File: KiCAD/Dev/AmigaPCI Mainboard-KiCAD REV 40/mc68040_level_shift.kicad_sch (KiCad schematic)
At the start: 26 parts, among them U801 74LVC1G17, U802 SN74LVC16T245DLR, U803 SN74LVC16T245DLR, U804 SN74LVC16T245DLR, U805 SN74LVC16T245DLR, U806 74LVC245, U807 74LVC245, U808 74LVC245, U809 74LVC245, U810 74LVC245, U811 74LVC245

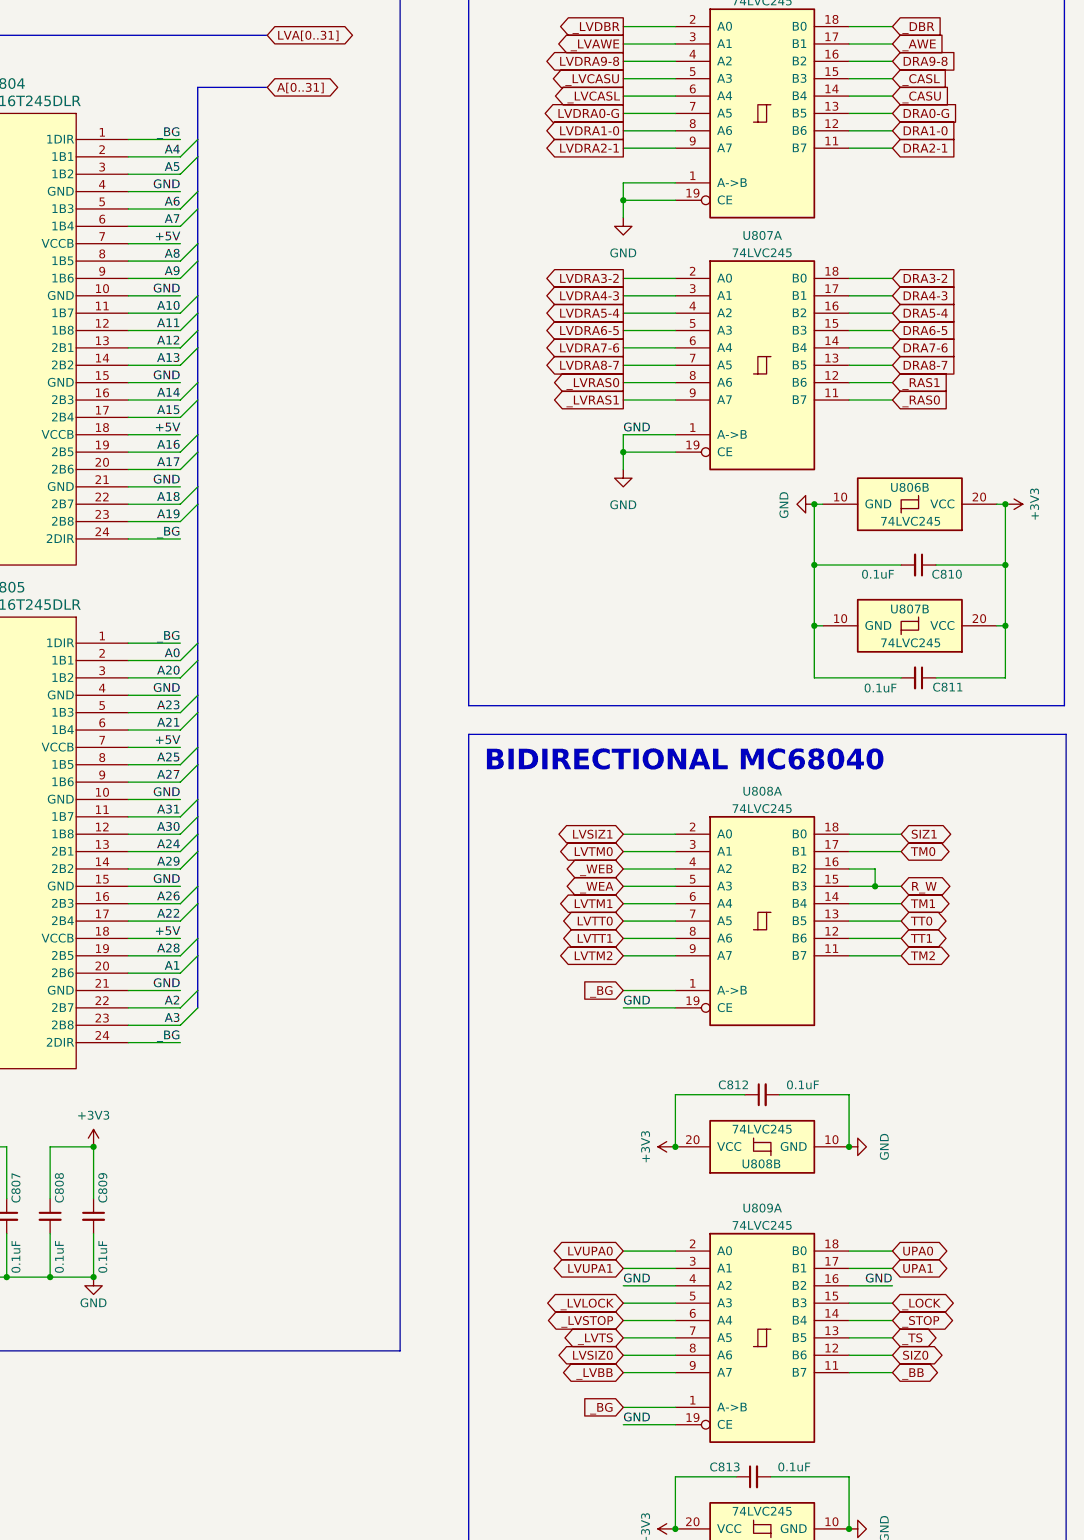
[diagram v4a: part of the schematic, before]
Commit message: AmigaPCI - Add BUSDIR signal, seperate from _BG.
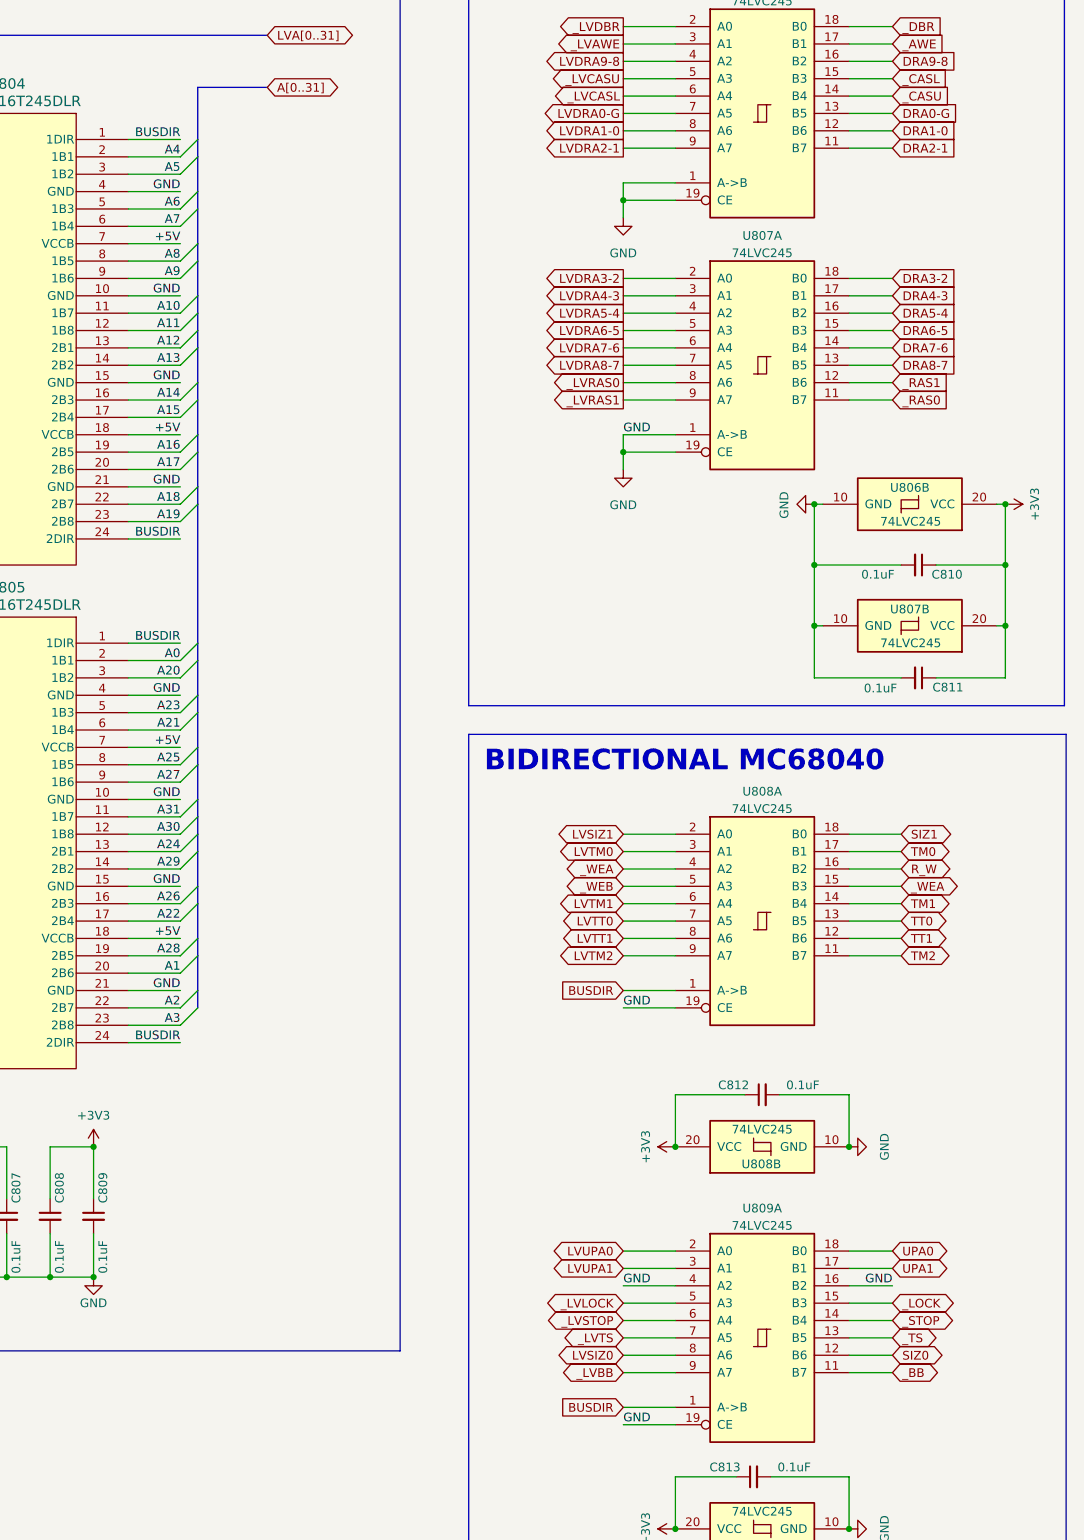
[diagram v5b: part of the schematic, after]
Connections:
- net R_W: no longer U808.15 (B3)
- net _WEA: now also U808.15 (B3), U808.4 (A2); no longer U808.5 (A3)
- net _WEB: now also U808.5 (A3); no longer U808.4 (A2)
- net _BG renamed BUSDIR
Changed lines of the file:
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@@
 		(color 0 0 0 0)
 	)
-	(junction
-		(at 271.78 160.02)
-		(diameter 0)
-		(color 0 0 0 0)
-	)
 	(bus_entry
 		(at 120.65 129.54)
@@
 		)
 	)
-	(wire
-		(pts
-			(xy 267.97 157.48) (xy 271.78 157.48)
-		)
-		(stroke
-			(width 0)
-			(type default)
-		)
-	)
 	(bus
 		(pts
@@
 		)
 	)
-	(wire
-		(pts
-			(xy 275.59 160.02) (xy 271.78 160.02)
-		)
-		(stroke
-			(width 0)
-			(type default)
-		)
-	)
 	(bus
 		(pts
@@
 	(wire
 		(pts
-			(xy 271.78 157.48) (xy 271.78 160.02)
-		)
-		(stroke
-			(width 0)
-			(type default)
-		)
-	)
-	(wire
-		(pts
 			(xy 81.28 149.86) (xy 74.93 149.86)
 		)
@@
 	(wire
 		(pts
-			(xy 271.78 160.02) (xy 267.97 160.02)
+			(xy 267.97 160.02) (xy 275.59 160.02)
 		)
 		(stroke
@@
 		)
 	)
+	(wire
+		(pts
+			(xy 275.59 157.48) (xy 267.97 157.48)
+		)
+		(stroke
+			(width 0)
+			(type default)
+		)
+	)
 	(bus
 		(pts
@@
 		)
 	)
-	(label "_BG"
+	(label "BUSDIR"
 		(at 170.18 50.8 180)
 		(fields_autoplaced yes)
@@
 		)
 	)
+	(label "GND"
+		(at 274.32 218.44 180)
+		(fields_autoplaced yes)
+		(effects
+			(font
+				(size 1.27 1.27)
+			)
+			(justify right bottom)
+		)
+	)
 	(label "A23"
 		(at 170.18 134.62 180)
@@
 		)
 	)
-	(label "_BG"
+	(label "BUSDIR"
 		(at 170.18 109.22 180)
 		(fields_autoplaced yes)
@@
 		)
 	)
+	(label "GND"
+		(at 234.95 218.44 0)
+		(fields_autoplaced yes)
+		(effects
+			(font
+				(size 1.27 1.27)
+			)
+			(justify left bottom)
+		)
+	)
 	(label "D30"
 		(at 81.28 177.8 180)
@@
 		)
 	)
-	(label "_BG"
+	(label "BUSDIR"
 		(at 170.18 124.46 180)
 		(fields_autoplaced yes)
@@
 		)
 	)
-	(label "GND"
-		(at 274.32 218.44 180)
-		(fields_autoplaced yes)
-		(effects
-			(font
-				(size 1.27 1.27)
-			)
-			(justify right bottom)
-		)
-	)
 	(label "UDB10"
 		(at 349.25 92.71 0)
@@
 		)
 	)
-	(label "_BG"
+	(label "BUSDIR"
 		(at 170.18 182.88 180)
 		(fields_autoplaced yes)
@@
 		)
 	)
-	(label "GND"
-		(at 234.95 218.44 0)
-		(fields_autoplaced yes)
-		(effects
-			(font
-				(size 1.27 1.27)
-			)
-			(justify left bottom)
-		)
-	)
 	(label "LVD5"
 		(at 31.75 71.12 0)
@@
 	(global_label "_WEB"
 		(shape bidirectional)
-		(at 234.95 157.48 180)
+		(at 234.95 160.02 180)
 		(effects
 			(font
@@
 		)
 		(property "Intersheetrefs" "${INTERSHEET_REFS}"
-			(at 226.06 157.353 0)
+			(at 226.06 159.893 0)
 			(effects
 				(font
@@
 		)
 	)
-	(global_label "_BG"
+	(global_label "BUSDIR"
 		(shape input)
 		(at 234.95 175.26 180)
@@
 		)
 		(property "Intersheetrefs" "${INTERSHEET_REFS}"
-			(at 228.4572 175.26 0)
+			(at 225.01 175.26 0)
 			(effects
 				(font
@@
 		)
 	)
+	(global_label "_WEA"
+		(shape bidirectional)
+		(at 275.59 160.02 0)
+		(effects
+			(font
+				(size 1.27 1.27)
+			)
+			(justify left)
+		)
+		(property "Intersheetrefs" "${INTERSHEET_REFS}"
+			(at 284.48 159.893 0)
+			(effects
+				(font
+					(size 1.27 1.27)
+				)
+				(justify left)
+			)
+		)
+	)
 	(global_label "_AWE"
 		(shape input)
@@
 	(global_label "R_W"
 		(shape bidirectional)
-		(at 275.59 160.02 0)
+		(at 275.59 157.48 0)
 		(effects
 			(font
@@
 		)
 		(property "Intersheetrefs" "${INTERSHEET_REFS}"
-			(at 281.813 160.02 0)
+			(at 281.813 157.48 0)
 			(effects
 				(font
@@
 		)
 	)
-	(global_label "_BG"
+	(global_label "BUSDIR"
 		(shape input)
 		(at 234.95 236.22 180)
@@
 		)
 		(property "Intersheetrefs" "${INTERSHEET_REFS}"
-			(at 228.4572 236.22 0)
+			(at 225.01 236.22 0)
 			(effects
 				(font
@@
 	(global_label "_WEA"
 		(shape bidirectional)
-		(at 234.95 160.02 180)
+		(at 234.95 157.48 180)
 		(effects
 			(font
@@
 		)
 		(property "Intersheetrefs" "${INTERSHEET_REFS}"
-			(at 226.06 159.893 0)
+			(at 226.06 157.353 0)
 			(effects
 				(font

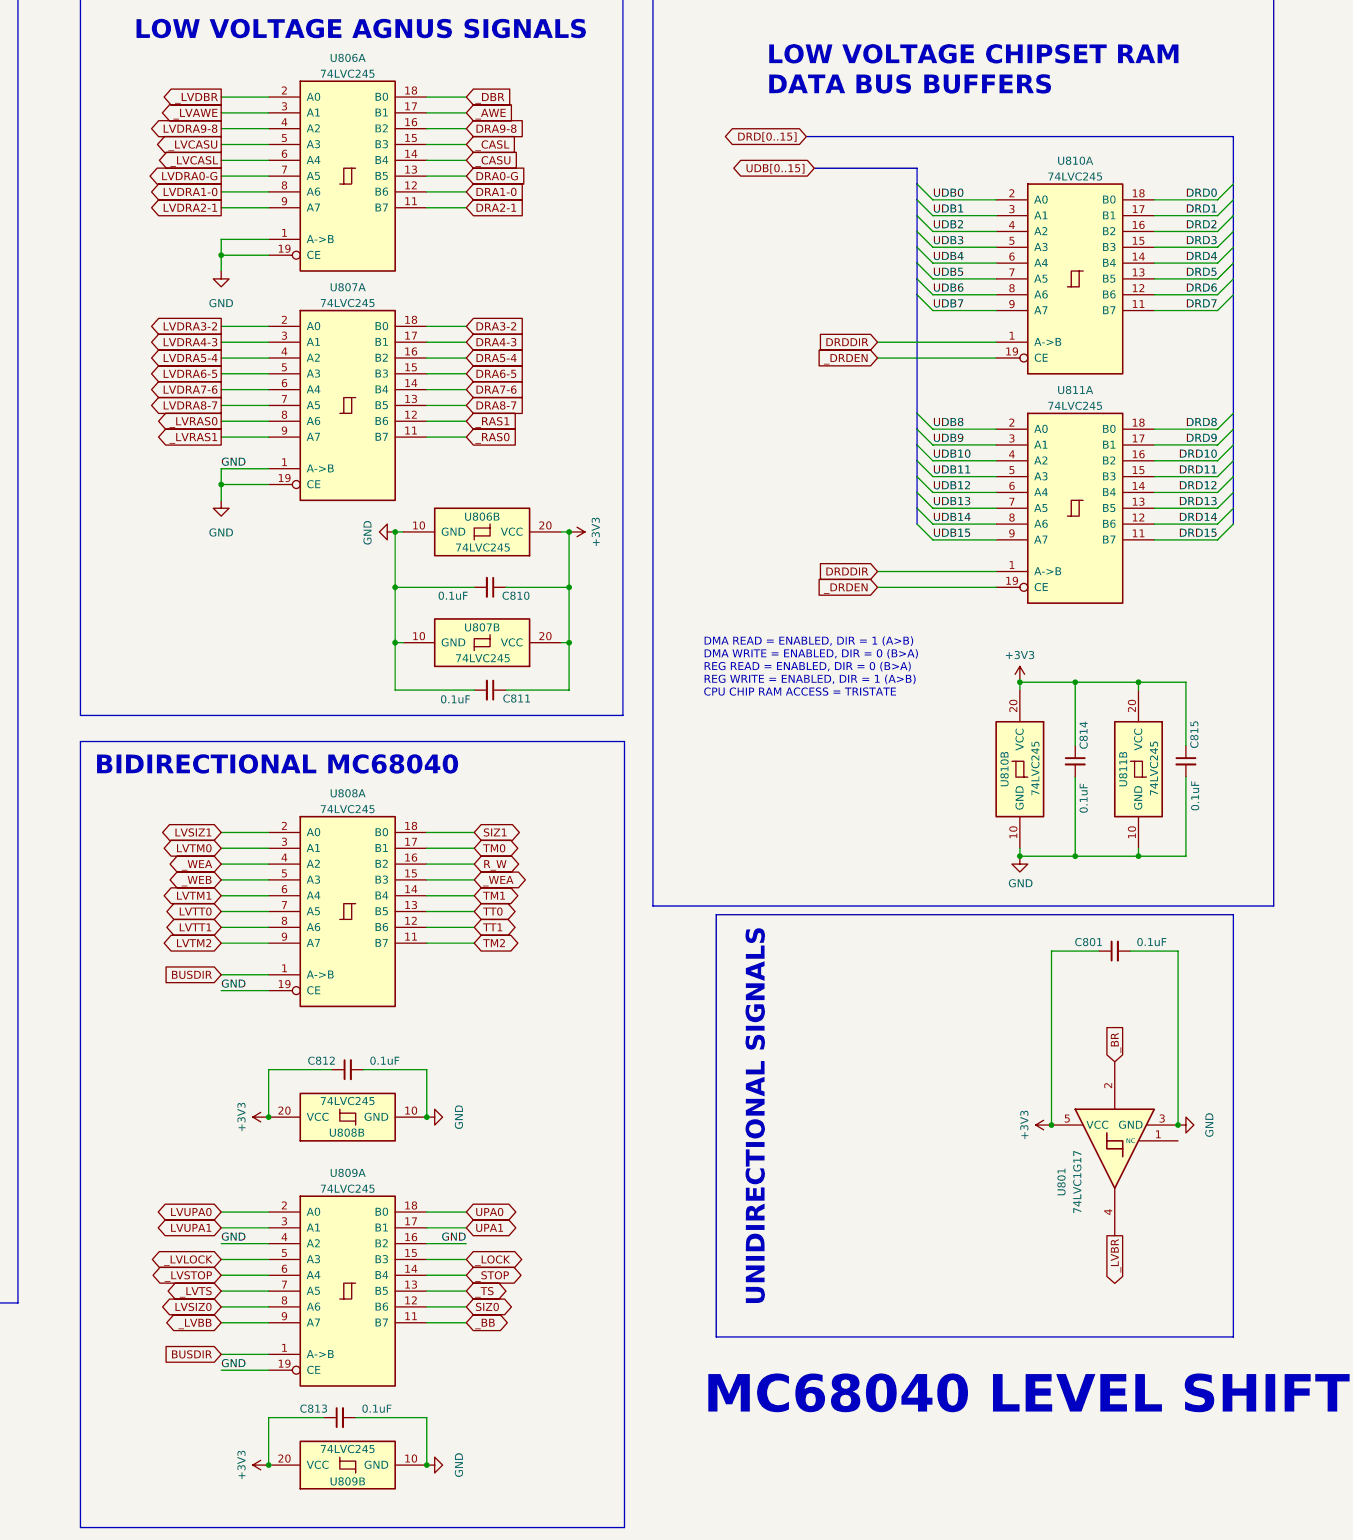
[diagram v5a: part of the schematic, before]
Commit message: AmigaPCI - swap U810 & U811 with SN74LVC16T245DLR
Drive Agnus DBR bus with TTL levels.
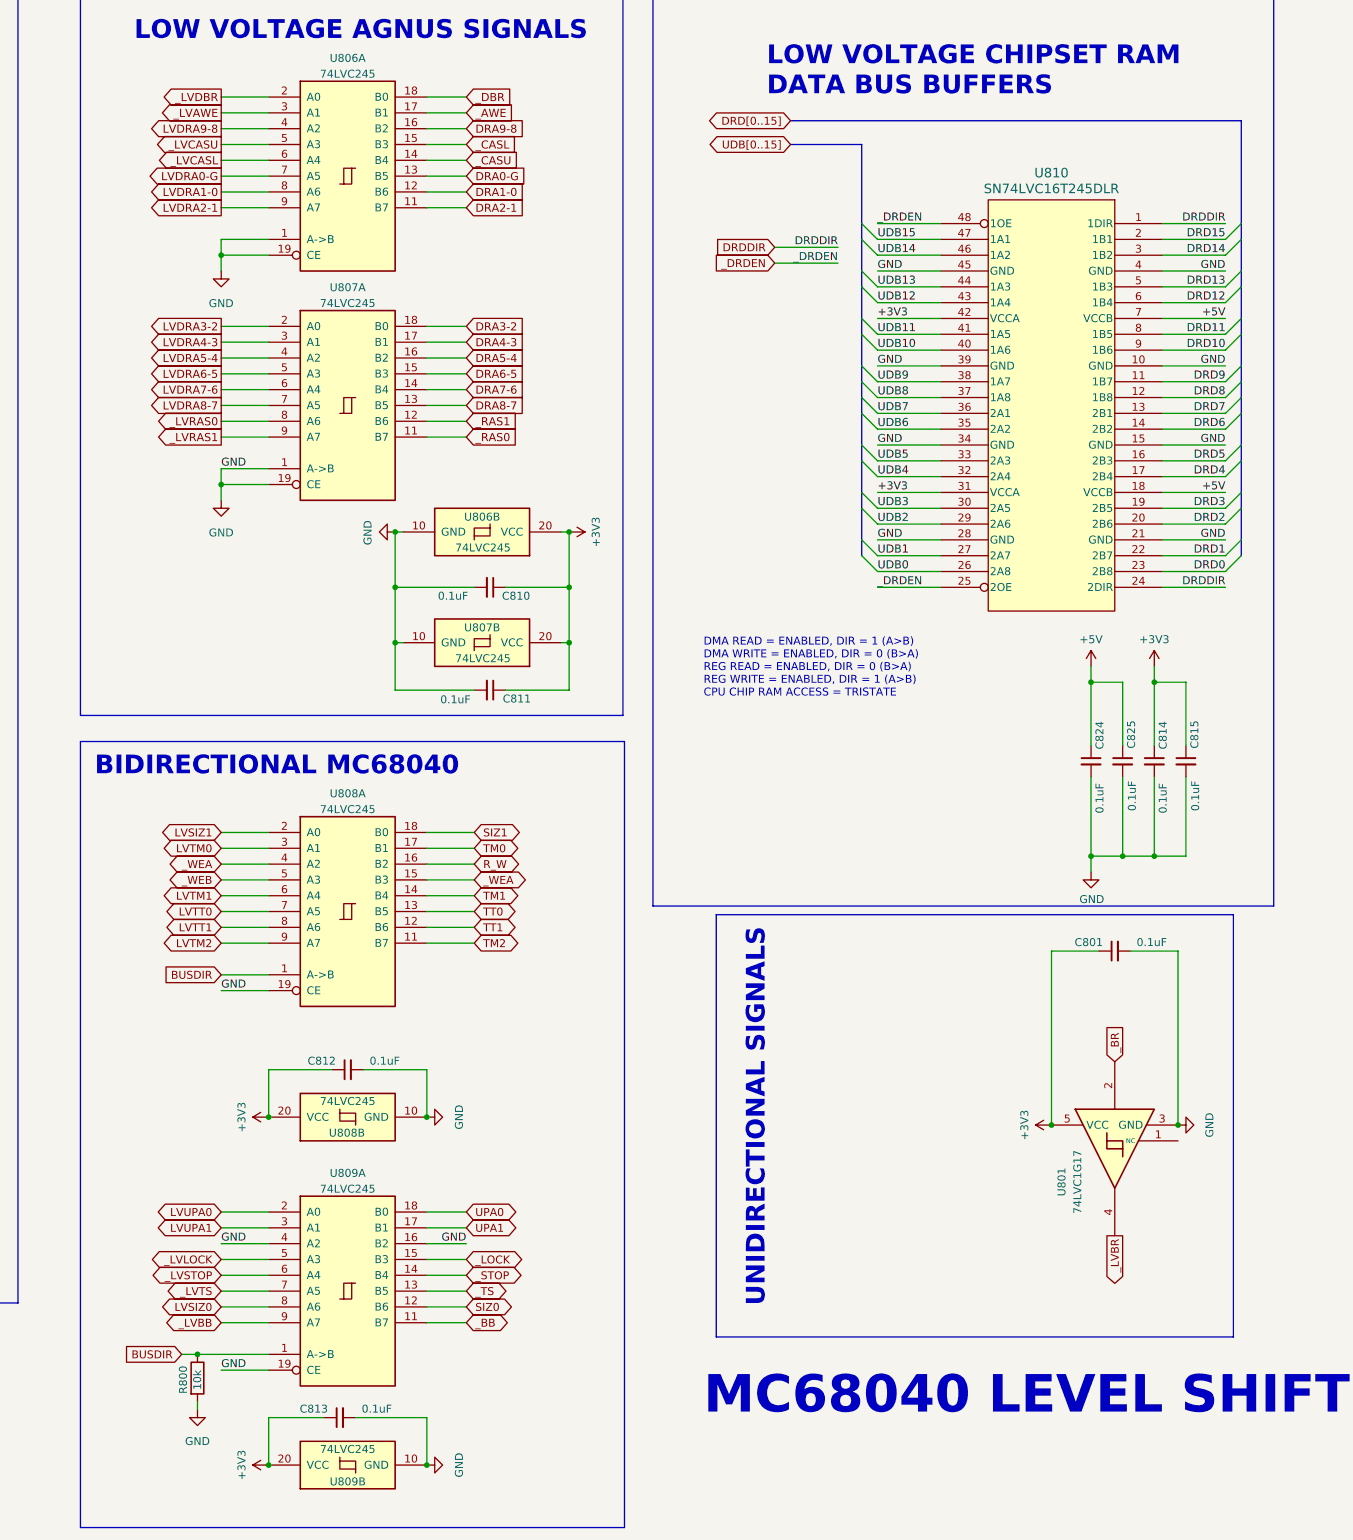
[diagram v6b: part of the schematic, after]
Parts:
- removed U810, U811: 74LVC245, Package_SO:TSSOP-20_4.4x6.5mm_P0.65mm, symbol AmigaPCI-Symbols:74LVC245
- added C824, C825: 0.1uF, Capacitor_SMD:C_0603_1608Metric, symbol Device:C_Small
- added R800: 10k, Resistor_SMD:R_0603_1608Metric, symbol Device:R
- added U810: SN74LVC16T245DLR, AmigaPCI:48-BSSOP, symbol AmigaPCI-Symbols:SN74LVC16T245DLR
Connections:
- net +3V3: now also U810.31 (VCCA), U810.42 (VCCA)
- net +5V: now also C824.1, C825.1, U810.18 (VCCB), U810.7 (VCCB)
- net BUSDIR: now also R800.1
- net DRD0: now also U810.23 (2B8)
- net DRD1: now also U810.22 (2B7)
- net DRD10: now also U810.9 (1B6)
- net DRD11: now also U810.8 (1B5)
- net DRD12: now also U810.6 (1B4)
- net DRD13: now also U810.5 (1B3)
- net DRD14: now also U810.3 (1B2)
- net DRD15: now also U810.2 (1B1)
- net DRD2: now also U810.20 (2B6)
- net DRD3: now also U810.19 (2B5)
- net DRD4: now also U810.17 (2B4)
- net DRD5: now also U810.16 (2B3)
- net DRD6: now also U810.14 (2B2)
- net DRD7: now also U810.13 (2B1)
- net DRD8: now also U810.12 (1B8)
- net DRD9: now also U810.11 (1B7)
- net DRDDIR: now also U810.1 (1DIR), U810.24 (2DIR)
- net GND: now also C824.2, C825.2, R800.2, U810.10 (GND), U810.15 (GND), U810.21 (GND), U810.28 (GND), U810.34 (GND), U810.39 (GND), U810.4 (GND), U810.45 (GND)
- net UDB0: now also U810.26 (2A8)
- net UDB1: now also U810.27 (2A7)
- net UDB10: now also U810.40 (1A6)
- net UDB11: now also U810.41 (1A5)
- net UDB12: now also U810.43 (1A4)
- net UDB13: now also U810.44 (1A3)
- net UDB14: now also U810.46 (1A2)
- net UDB15: now also U810.47 (1A1)
- net UDB2: now also U810.29 (2A6)
- net UDB3: now also U810.30 (2A5)
- net UDB4: now also U810.32 (2A4)
- net UDB5: now also U810.33 (2A3)
- net UDB6: now also U810.35 (2A2)
- net UDB7: now also U810.36 (2A1)
- net UDB8: now also U810.37 (1A8)
- net UDB9: now also U810.38 (1A7)
- net _DRDEN: now also U810.25 (2OE), U810.48 (1OE)
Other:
- moved on the sheet: C814
